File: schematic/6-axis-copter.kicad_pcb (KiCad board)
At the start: 2 copper layers, 98 x 98 mm, 188 parts

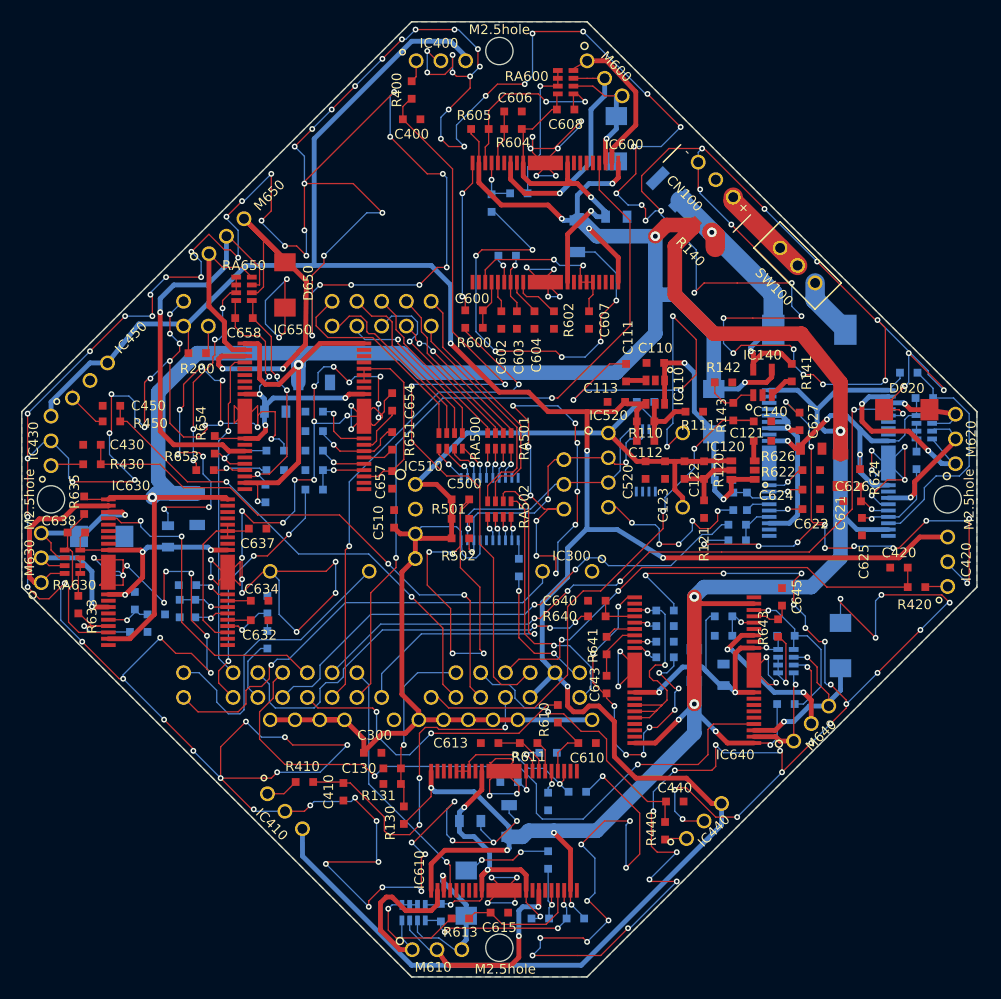
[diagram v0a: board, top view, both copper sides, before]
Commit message: 基板製造メーカー(P板.com)の指摘を元にPCBボード図を修正
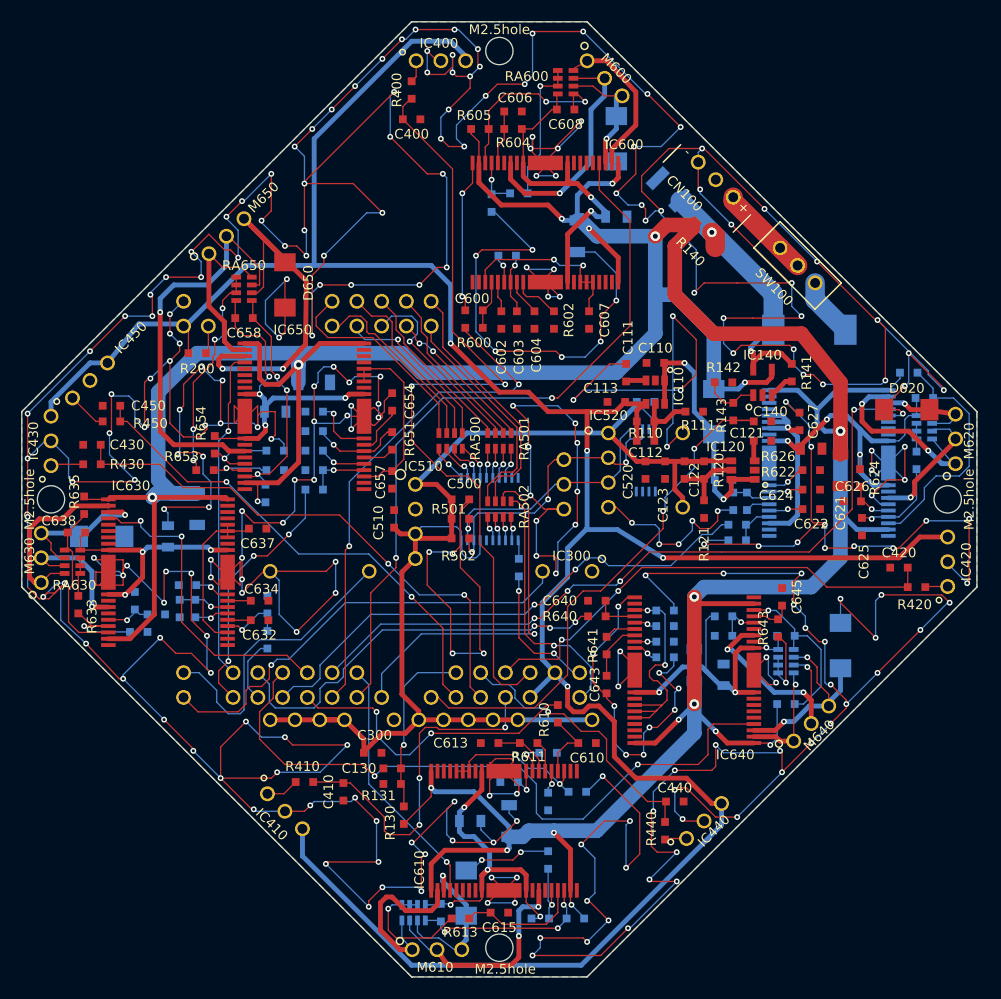
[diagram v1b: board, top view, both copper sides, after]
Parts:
- M600, M610, M620, M630, M640, M650: footprint L2508A-3500 -> HK-AP05
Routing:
- net GND: track 1449.4 -> 1459.4 mm
